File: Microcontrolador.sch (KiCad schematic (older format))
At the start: 16 parts, among them U4 EFM32TG11B120F128GM32, Y1 Crystal, Y2 Crystal

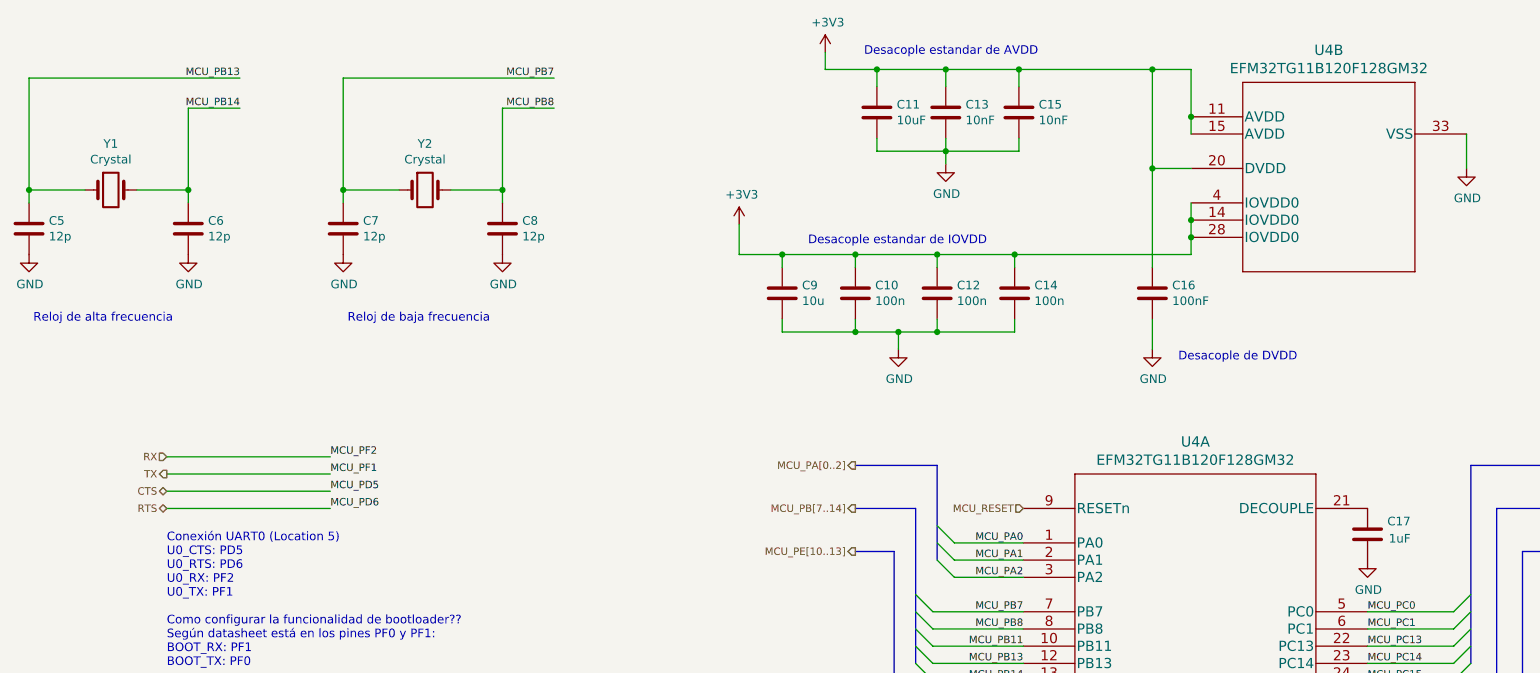
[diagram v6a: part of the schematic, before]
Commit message: Issue #2: Primer acercamiento al diseño de la PCB
Se modificaron los conectores externos de los pines GPIOs (para no
exponer los que se conectan a los cristales) y se realizó la
distribución inicial de componentes en la placa (sin conectarlos)
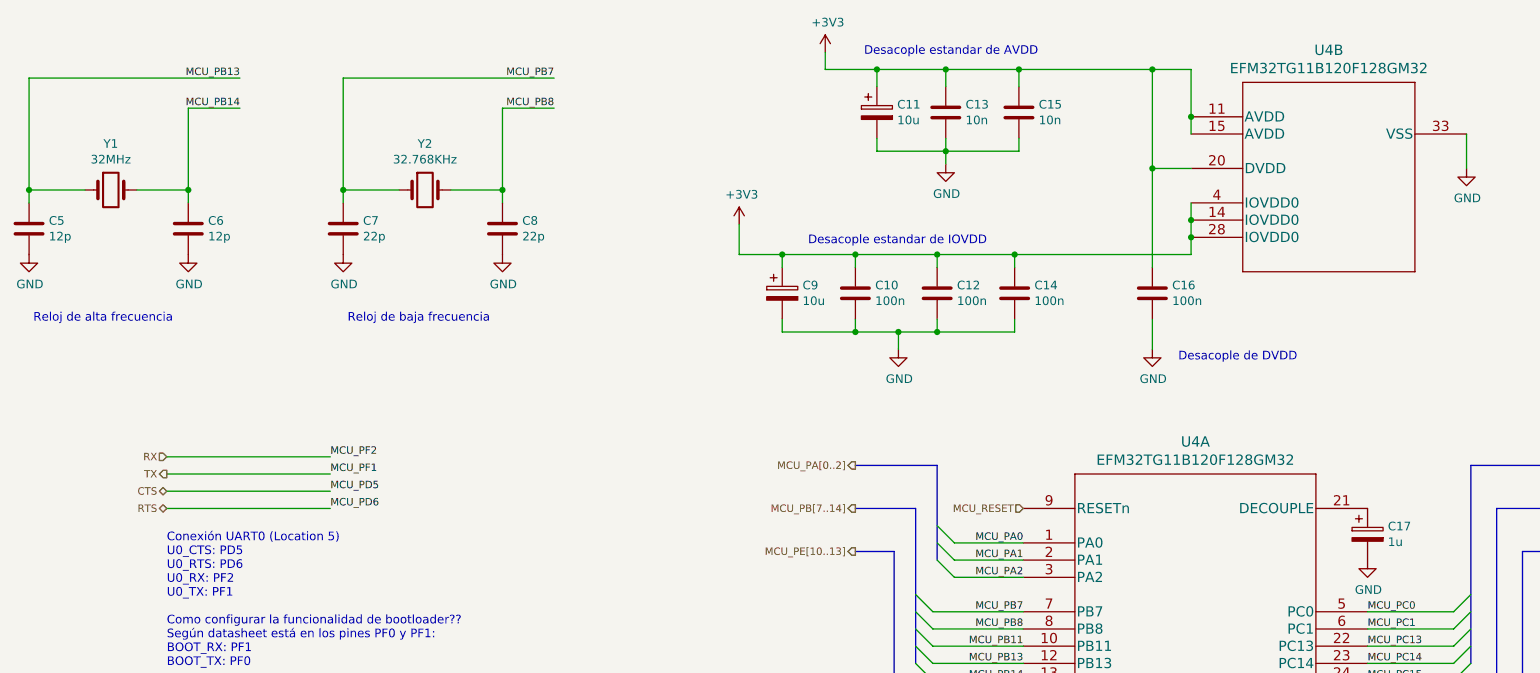
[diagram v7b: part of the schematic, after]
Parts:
- removed C11: 10uF, symbol Device:C
- removed C17: 1uF, symbol Device:C
- removed C9: 10u, symbol Device:C
- added C11, C9: 10u, Capacitor_THT:CP_Radial_D5.0mm_P2.50mm, symbol Device:CP
- added C17: 1u, Capacitor_THT:CP_Radial_D5.0mm_P2.50mm, symbol Device:CP
- C10, C12, C14, C5, C6: footprint (none) -> Capacitor_SMD:C_0603_1608Metric_Pad1.05x0.95mm_HandSolder
- C13, C15: value 10nF -> 10n; footprint (none) -> Capacitor_SMD:C_0603_1608Metric_Pad1.05x0.95mm_HandSolder
- C16: value 100nF -> 100n; footprint (none) -> Capacitor_SMD:C_0603_1608Metric_Pad1.05x0.95mm_HandSolder
- C7, C8: value 12p -> 22p; footprint (none) -> Capacitor_THT:C_Disc_D3.0mm_W1.6mm_P2.50mm
- Y1: value Crystal -> 32MHz; footprint (none) -> Crystal:Crystal_SMD_ECS_CSM3X-2Pin_7.6x4.1mm
- Y2: value Crystal -> 32.768KHz; footprint (none) -> Crystal:Crystal_AT310_D3.0mm_L10.0mm_Horizontal
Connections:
- net +3V3: now also C11.1, C9.1
- net GND: now also C11.2, C17.2, C9.2
- net at U4.21 (DECOUPLE): now also C17.1
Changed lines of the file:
@@
 $EndDescr
-$Comp
-L Device:C C?
-U 1 1 5F4D7858
-P 9050 3675
-AR Path="/5F4D7858" Ref="C?"  Part="1"
-AR Path="/5F4D1FFB/5F4D7858" Ref="C17"  Part="1"
-F 0 "C17" H 8800 3600 50  0000 L CNN
-F 1 "1uF" H 8800 3700 50  0000 L CNN
-F 2 "" H 9088 3525 50  0001 C CNN
-F 3 "~" H 9050 3675 50  0001 C CNN
-	1    9050 3675
-	-1   0    0    1
-$EndComp
 $Comp
 L EFM32TG11B120F128GM32:EFM32TG11B120F128GM32 U?
@@
 AR Path="/5F4D1FFB/5F4D786A" Ref="C13"  Part="1"
 F 0 "C13" H 6715 1271 50  0000 L CNN
-F 1 "10nF" H 6715 1180 50  0000 L CNN
-F 2 "" H 6638 1075 50  0001 C CNN
+F 1 "10n" H 6715 1180 50  0000 L CNN
+F 2 "Capacitor_SMD:C_0603_1608Metric_Pad1.05x0.95mm_HandSolder" H 6638 1075 50  0001 C CNN
 F 3 "~" H 6600 1225 50  0001 C CNN
 	1    6600 1225
-	1    0    0    -1
-$EndComp
-$Comp
-L Device:C C?
-U 1 1 5F4D7870
-P 6200 1225
-AR Path="/5F4D7870" Ref="C?"  Part="1"
-AR Path="/5F4D1FFB/5F4D7870" Ref="C11"  Part="1"
-F 0 "C11" H 6315 1271 50  0000 L CNN
-F 1 "10uF" H 6315 1180 50  0000 L CNN
-F 2 "" H 6238 1075 50  0001 C CNN
-F 3 "~" H 6200 1225 50  0001 C CNN
-	1    6200 1225
 	1    0    0    -1
 $EndComp
@@
 F 0 "C10" H 6190 2321 50  0000 L CNN
 F 1 "100n" H 6190 2230 50  0000 L CNN
-F 2 "" H 6113 2125 50  0001 C CNN
+F 2 "Capacitor_SMD:C_0603_1608Metric_Pad1.05x0.95mm_HandSolder" H 6113 2125 50  0001 C CNN
 F 3 "~" H 6075 2275 50  0001 C CNN
 	1    6075 2275
@@
 AR Path="/5F4D1FFB/5F4D7888" Ref="C16"  Part="1"
 F 0 "C16" H 7915 2321 50  0000 L CNN
-F 1 "100nF" H 7915 2230 50  0000 L CNN
-F 2 "" H 7838 2125 50  0001 C CNN
+F 1 "100n" H 7915 2230 50  0000 L CNN
+F 2 "Capacitor_SMD:C_0603_1608Metric_Pad1.05x0.95mm_HandSolder" H 7838 2125 50  0001 C CNN
 F 3 "~" H 7800 2275 50  0001 C CNN
 	1    7800 2275
@@
 AR Path="/5F4D1FFB/5F4D788E" Ref="C15"  Part="1"
 F 0 "C15" H 7140 1271 50  0000 L CNN
-F 1 "10nF" H 7140 1180 50  0000 L CNN
-F 2 "" H 7063 1075 50  0001 C CNN
+F 1 "10n" H 7140 1180 50  0000 L CNN
+F 2 "Capacitor_SMD:C_0603_1608Metric_Pad1.05x0.95mm_HandSolder" H 7063 1075 50  0001 C CNN
 F 3 "~" H 7025 1225 50  0001 C CNN
 	1    7025 1225
@@
 P 1750 1675
 F 0 "Y1" H 1750 1943 50  0000 C CNN
-F 1 "Crystal" H 1750 1852 50  0000 C CNN
-F 2 "" H 1750 1675 50  0001 C CNN
+F 1 "32MHz" H 1750 1852 50  0000 C CNN
+F 2 "Crystal:Crystal_SMD_ECS_CSM3X-2Pin_7.6x4.1mm" H 1750 1675 50  0001 C CNN
 F 3 "~" H 1750 1675 50  0001 C CNN
 	1    1750 1675
@@
 F 0 "C5" H 1390 1946 50  0000 L CNN
 F 1 "12p" H 1390 1855 50  0000 L CNN
-F 2 "" H 1313 1750 50  0001 C CNN
+F 2 "Capacitor_SMD:C_0603_1608Metric_Pad1.05x0.95mm_HandSolder" H 1313 1750 50  0001 C CNN
 F 3 "~" H 1275 1900 50  0001 C CNN
 	1    1275 1900
@@
 F 0 "C6" H 2315 1946 50  0000 L CNN
 F 1 "12p" H 2315 1855 50  0000 L CNN
-F 2 "" H 2238 1750 50  0001 C CNN
+F 2 "Capacitor_SMD:C_0603_1608Metric_Pad1.05x0.95mm_HandSolder" H 2238 1750 50  0001 C CNN
 F 3 "~" H 2200 1900 50  0001 C CNN
 	1    2200 1900
@@
 F 0 "C12" H 6665 2321 50  0000 L CNN
 F 1 "100n" H 6665 2230 50  0000 L CNN
-F 2 "" H 6588 2125 50  0001 C CNN
+F 2 "Capacitor_SMD:C_0603_1608Metric_Pad1.05x0.95mm_HandSolder" H 6588 2125 50  0001 C CNN
 F 3 "~" H 6550 2275 50  0001 C CNN
 	1    6550 2275
@@
 F 0 "C14" H 7115 2321 50  0000 L CNN
 F 1 "100n" H 7115 2230 50  0000 L CNN
-F 2 "" H 7038 2125 50  0001 C CNN
+F 2 "Capacitor_SMD:C_0603_1608Metric_Pad1.05x0.95mm_HandSolder" H 7038 2125 50  0001 C CNN
 F 3 "~" H 7000 2275 50  0001 C CNN
 	1    7000 2275
@@
 Wire Wire Line
 	7800 1550 8025 1550
-$Comp
-L Device:C C?
-U 1 1 5F50D7A2
-P 5650 2275
-AR Path="/5F50D7A2" Ref="C?"  Part="1"
-AR Path="/5F4D1FFB/5F50D7A2" Ref="C9"  Part="1"
-F 0 "C9" H 5765 2321 50  0000 L CNN
-F 1 "10u" H 5765 2230 50  0000 L CNN
-F 2 "" H 5688 2125 50  0001 C CNN
-F 3 "~" H 5650 2275 50  0001 C CNN
-	1    5650 2275
-	1    0    0    -1
-$EndComp
 Wire Wire Line
 	8025 1750 8025 1850
@@
 P 3575 1675
 F 0 "Y2" H 3575 1943 50  0000 C CNN
-F 1 "Crystal" H 3575 1852 50  0000 C CNN
-F 2 "" H 3575 1675 50  0001 C CNN
+F 1 "32.768KHz" H 3575 1852 50  0000 C CNN
+F 2 "Crystal:Crystal_AT310_D3.0mm_L10.0mm_Horizontal" H 3575 1675 50  0001 C CNN
 F 3 "~" H 3575 1675 50  0001 C CNN
 	1    3575 1675
@@
 P 3100 1900
 F 0 "C7" H 3215 1946 50  0000 L CNN
-F 1 "12p" H 3215 1855 50  0000 L CNN
-F 2 "" H 3138 1750 50  0001 C CNN
+F 1 "22p" H 3215 1855 50  0000 L CNN
+F 2 "Capacitor_THT:C_Disc_D3.0mm_W1.6mm_P2.50mm" H 3138 1750 50  0001 C CNN
 F 3 "~" H 3100 1900 50  0001 C CNN
 	1    3100 1900
@@
 P 4025 1900
 F 0 "C8" H 4140 1946 50  0000 L CNN
-F 1 "12p" H 4140 1855 50  0000 L CNN
-F 2 "" H 4063 1750 50  0001 C CNN
+F 1 "22p" H 4140 1855 50  0000 L CNN
+F 2 "Capacitor_THT:C_Disc_D3.0mm_W1.6mm_P2.50mm" H 4063 1750 50  0001 C CNN
 F 3 "~" H 4025 1900 50  0001 C CNN
 	1    4025 1900
@@
 Wire Bus Line
 	6425 3525 6425 4425
+$Comp
+L Device:CP C11
+U 1 1 5F69D076
+P 6200 1225
+F 0 "C11" H 6318 1271 50  0000 L CNN
+F 1 "10u" H 6318 1180 50  0000 L CNN
+F 2 "Capacitor_THT:CP_Radial_D5.0mm_P2.50mm" H 6238 1075 50  0001 C CNN
+F 3 "~" H 6200 1225 50  0001 C CNN
+	1    6200 1225
+	1    0    0    -1
+$EndComp
+$Comp
+L Device:CP C9
+U 1 1 5F69E612
+P 5650 2275
+F 0 "C9" H 5768 2321 50  0000 L CNN
+F 1 "10u" H 5768 2230 50  0000 L CNN
+F 2 "Capacitor_THT:CP_Radial_D5.0mm_P2.50mm" H 5688 2125 50  0001 C CNN
+F 3 "~" H 5650 2275 50  0001 C CNN
+	1    5650 2275
+	1    0    0    -1
+$EndComp
+$Comp
+L Device:CP C17
+U 1 1 5F6F5B46
+P 9050 3675
+F 0 "C17" H 9168 3721 50  0000 L CNN
+F 1 "1u" H 9168 3630 50  0000 L CNN
+F 2 "Capacitor_THT:CP_Radial_D5.0mm_P2.50mm" H 9088 3525 50  0001 C CNN
+F 3 "~" H 9050 3675 50  0001 C CNN
+	1    9050 3675
+	1    0    0    -1
+$EndComp
 $EndSCHEMATC

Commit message: Issue #2: PCB lista para primera prueba de concepto
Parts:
- removed C11, C9: 10u, Capacitor_THT:CP_Radial_D5.0mm_P2.50mm, symbol Device:CP
- removed C17: 1u, Capacitor_THT:CP_Radial_D5.0mm_P2.50mm, symbol Device:CP
- added C11, C9: 10u, Capacitor_SMD:C_1206_3216Metric_Pad1.42x1.75mm_HandSolder, symbol Device:C
- added C17: 1u, Capacitor_SMD:C_1206_3216Metric_Pad1.42x1.75mm_HandSolder, symbol Device:C
- C10, C12, C13, C14, C15, C16: footprint Capacitor_SMD:C_0603_1608Metric_Pad1.05x0.95mm_HandSolder -> Capacitor_SMD:C_1206_3216Metric_Pad1.42x1.75mm_HandSolder
- C5, C6: footprint Capacitor_SMD:C_0603_1608Metric_Pad1.05x0.95mm_HandSolder -> Capacitor_SMD:C_0805_2012Metric_Pad1.15x1.40mm_HandSolder
- C7, C8: footprint Capacitor_THT:C_Disc_D3.0mm_W1.6mm_P2.50mm -> Capacitor_SMD:C_0805_2012Metric_Pad1.15x1.40mm_HandSolder
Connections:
- net +3V3: now also C11.1, C9.1
- net GND: now also C8.1, C11.2, C17.2, C9.2; no longer C8.2
- net MCU_PB8: now also C8.2; no longer C8.1
- net at U4.21 (DECOUPLE): now also C17.1
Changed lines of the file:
@@
 $Descr A4 11693 8268
 encoding utf-8
-Sheet 4 4
+Sheet 2 4
 Title "Placa de Desarrollo EFM32 - MCU ARM"
 Date "2020-08-30"
@@
 F 0 "C13" H 6715 1271 50  0000 L CNN
 F 1 "10n" H 6715 1180 50  0000 L CNN
-F 2 "Capacitor_SMD:C_0603_1608Metric_Pad1.05x0.95mm_HandSolder" H 6638 1075 50  0001 C CNN
+F 2 "Capacitor_SMD:C_1206_3216Metric_Pad1.42x1.75mm_HandSolder" H 6638 1075 50  0001 C CNN
 F 3 "~" H 6600 1225 50  0001 C CNN
 	1    6600 1225
@@
 F 0 "C10" H 6190 2321 50  0000 L CNN
 F 1 "100n" H 6190 2230 50  0000 L CNN
-F 2 "Capacitor_SMD:C_0603_1608Metric_Pad1.05x0.95mm_HandSolder" H 6113 2125 50  0001 C CNN
+F 2 "Capacitor_SMD:C_1206_3216Metric_Pad1.42x1.75mm_HandSolder" H 6113 2125 50  0001 C CNN
 F 3 "~" H 6075 2275 50  0001 C CNN
 	1    6075 2275
@@
 F 0 "C16" H 7915 2321 50  0000 L CNN
 F 1 "100n" H 7915 2230 50  0000 L CNN
-F 2 "Capacitor_SMD:C_0603_1608Metric_Pad1.05x0.95mm_HandSolder" H 7838 2125 50  0001 C CNN
+F 2 "Capacitor_SMD:C_1206_3216Metric_Pad1.42x1.75mm_HandSolder" H 7838 2125 50  0001 C CNN
 F 3 "~" H 7800 2275 50  0001 C CNN
 	1    7800 2275
@@
 F 0 "C15" H 7140 1271 50  0000 L CNN
 F 1 "10n" H 7140 1180 50  0000 L CNN
-F 2 "Capacitor_SMD:C_0603_1608Metric_Pad1.05x0.95mm_HandSolder" H 7063 1075 50  0001 C CNN
+F 2 "Capacitor_SMD:C_1206_3216Metric_Pad1.42x1.75mm_HandSolder" H 7063 1075 50  0001 C CNN
 F 3 "~" H 7025 1225 50  0001 C CNN
 	1    7025 1225
@@
 F 0 "C5" H 1390 1946 50  0000 L CNN
 F 1 "12p" H 1390 1855 50  0000 L CNN
-F 2 "Capacitor_SMD:C_0603_1608Metric_Pad1.05x0.95mm_HandSolder" H 1313 1750 50  0001 C CNN
+F 2 "Capacitor_SMD:C_0805_2012Metric_Pad1.15x1.40mm_HandSolder" H 1313 1750 50  0001 C CNN
 F 3 "~" H 1275 1900 50  0001 C CNN
 	1    1275 1900
@@
 F 0 "C6" H 2315 1946 50  0000 L CNN
 F 1 "12p" H 2315 1855 50  0000 L CNN
-F 2 "Capacitor_SMD:C_0603_1608Metric_Pad1.05x0.95mm_HandSolder" H 2238 1750 50  0001 C CNN
+F 2 "Capacitor_SMD:C_0805_2012Metric_Pad1.15x1.40mm_HandSolder" H 2238 1750 50  0001 C CNN
 F 3 "~" H 2200 1900 50  0001 C CNN
 	1    2200 1900
@@
 F 0 "C12" H 6665 2321 50  0000 L CNN
 F 1 "100n" H 6665 2230 50  0000 L CNN
-F 2 "Capacitor_SMD:C_0603_1608Metric_Pad1.05x0.95mm_HandSolder" H 6588 2125 50  0001 C CNN
+F 2 "Capacitor_SMD:C_1206_3216Metric_Pad1.42x1.75mm_HandSolder" H 6588 2125 50  0001 C CNN
 F 3 "~" H 6550 2275 50  0001 C CNN
 	1    6550 2275
@@
 F 0 "C14" H 7115 2321 50  0000 L CNN
 F 1 "100n" H 7115 2230 50  0000 L CNN
-F 2 "Capacitor_SMD:C_0603_1608Metric_Pad1.05x0.95mm_HandSolder" H 7038 2125 50  0001 C CNN
+F 2 "Capacitor_SMD:C_1206_3216Metric_Pad1.42x1.75mm_HandSolder" H 7038 2125 50  0001 C CNN
 F 3 "~" H 7000 2275 50  0001 C CNN
 	1    7000 2275
@@
 F 0 "C7" H 3215 1946 50  0000 L CNN
 F 1 "22p" H 3215 1855 50  0000 L CNN
-F 2 "Capacitor_THT:C_Disc_D3.0mm_W1.6mm_P2.50mm" H 3138 1750 50  0001 C CNN
+F 2 "Capacitor_SMD:C_0805_2012Metric_Pad1.15x1.40mm_HandSolder" H 3138 1750 50  0001 C CNN
 F 3 "~" H 3100 1900 50  0001 C CNN
 	1    3100 1900
@@
 F 0 "C8" H 4140 1946 50  0000 L CNN
 F 1 "22p" H 4140 1855 50  0000 L CNN
-F 2 "Capacitor_THT:C_Disc_D3.0mm_W1.6mm_P2.50mm" H 4063 1750 50  0001 C CNN
+F 2 "Capacitor_SMD:C_0805_2012Metric_Pad1.15x1.40mm_HandSolder" H 4063 1750 50  0001 C CNN
 F 3 "~" H 4025 1900 50  0001 C CNN
 	1    4025 1900
-	1    0    0    -1
+	1    0    0    1
 $EndComp
 Text Label 4325 1200 2    43   ~ 0
@@
 Text Notes 1500 6700 0    59   ~ 0
 DOCUMENTACION DE REFERENCIA\n=====================\n\nhttps://www.silabs.com/support/training/efm32-series-0-getting-started\n\nhttps://docs.silabs.com/mcu/5.8/efm32tg11/\n
-Wire Bus Line
-	6550 3275 6550 3825
-Wire Bus Line
-	9950 3775 9950 5325
-Wire Bus Line
-	9800 3525 9800 4925
-Wire Bus Line
-	9650 3275 9650 4425
-Wire Bus Line
-	6300 3775 6300 4925
-Wire Bus Line
-	6425 3525 6425 4425
-$Comp
-L Device:CP C11
-U 1 1 5F69D076
+$Comp
+L Device:C C?
+U 1 1 5F6CCD4E
 P 6200 1225
-F 0 "C11" H 6318 1271 50  0000 L CNN
-F 1 "10u" H 6318 1180 50  0000 L CNN
-F 2 "Capacitor_THT:CP_Radial_D5.0mm_P2.50mm" H 6238 1075 50  0001 C CNN
+AR Path="/5F6CCD4E" Ref="C?"  Part="1"
+AR Path="/5F4D1FFB/5F6CCD4E" Ref="C11"  Part="1"
+F 0 "C11" H 6315 1271 50  0000 L CNN
+F 1 "10u" H 6315 1180 50  0000 L CNN
+F 2 "Capacitor_SMD:C_1206_3216Metric_Pad1.42x1.75mm_HandSolder" H 6238 1075 50  0001 C CNN
 F 3 "~" H 6200 1225 50  0001 C CNN
 	1    6200 1225
@@
 $EndComp
 $Comp
-L Device:CP C9
-U 1 1 5F69E612
+L Device:C C17
+U 1 1 5F6CD9EF
+P 9050 3675
+F 0 "C17" H 9165 3721 50  0000 L CNN
+F 1 "1u" H 9165 3630 50  0000 L CNN
+F 2 "Capacitor_SMD:C_1206_3216Metric_Pad1.42x1.75mm_HandSolder" H 9088 3525 50  0001 C CNN
+F 3 "~" H 9050 3675 50  0001 C CNN
+	1    9050 3675
+	1    0    0    -1
+$EndComp
+$Comp
+L Device:C C?
+U 1 1 5F6CE4E2
 P 5650 2275
-F 0 "C9" H 5768 2321 50  0000 L CNN
-F 1 "10u" H 5768 2230 50  0000 L CNN
-F 2 "Capacitor_THT:CP_Radial_D5.0mm_P2.50mm" H 5688 2125 50  0001 C CNN
+AR Path="/5F6CE4E2" Ref="C?"  Part="1"
+AR Path="/5F4D1FFB/5F6CE4E2" Ref="C9"  Part="1"
+F 0 "C9" H 5765 2321 50  0000 L CNN
+F 1 "10u" H 5765 2230 50  0000 L CNN
+F 2 "Capacitor_SMD:C_1206_3216Metric_Pad1.42x1.75mm_HandSolder" H 5688 2125 50  0001 C CNN
 F 3 "~" H 5650 2275 50  0001 C CNN
 	1    5650 2275
 	1    0    0    -1
 $EndComp
-$Comp
-L Device:CP C17
-U 1 1 5F6F5B46
-P 9050 3675
-F 0 "C17" H 9168 3721 50  0000 L CNN
-F 1 "1u" H 9168 3630 50  0000 L CNN
-F 2 "Capacitor_THT:CP_Radial_D5.0mm_P2.50mm" H 9088 3525 50  0001 C CNN
-F 3 "~" H 9050 3675 50  0001 C CNN
-	1    9050 3675
-	1    0    0    -1
-$EndComp
+Wire Bus Line
+	6550 3275 6550 3825
+Wire Bus Line
+	9950 3775 9950 5325
+Wire Bus Line
+	9800 3525 9800 4925
+Wire Bus Line
+	9650 3275 9650 4425
+Wire Bus Line
+	6300 3775 6300 4925
+Wire Bus Line
+	6425 3525 6425 4425
 $EndSCHEMATC
